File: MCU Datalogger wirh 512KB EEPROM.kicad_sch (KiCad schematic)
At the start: 0 parts

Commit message: Added required symbols for the schematic design.
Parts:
- added BT1: Battery, symbol Device:Battery
- added C1, C2, C3, C4: C, symbol Device:C
- added C5: C_Polarized, symbol Device:C_Polarized
- added D1, D2: LED, symbol Device:LED
- added H1, H2, H3, H4: MountingHole, symbol Mechanical:MountingHole
- added IC1: ~, symbol ATMEGA328P-AU:ATMEGA328P-AU
- added R1, R2, R3, R4, R5, R6: R, symbol Device:R
- added U1, U2: 24LC1025, symbol Memory_EEPROM:24LC1025
- added U3: ~, symbol DS1337S+:DS1337S
- added Y1, Y2: Crystal, symbol Device:Crystal
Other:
- added sheet connectors (connectors.kicad_sch)

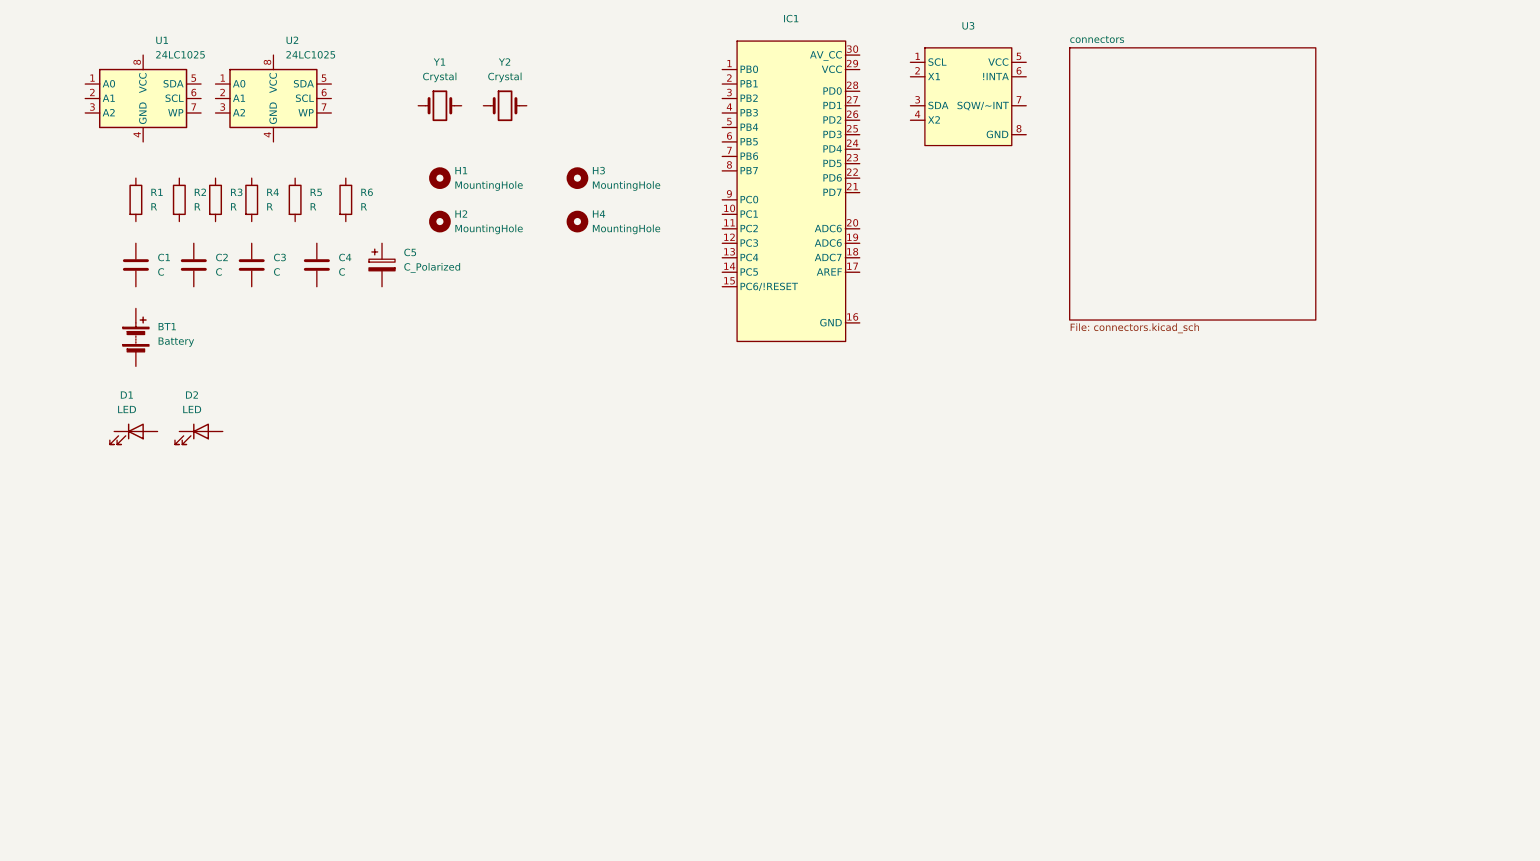
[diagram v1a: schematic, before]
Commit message: Arranged the placement of the symbols.
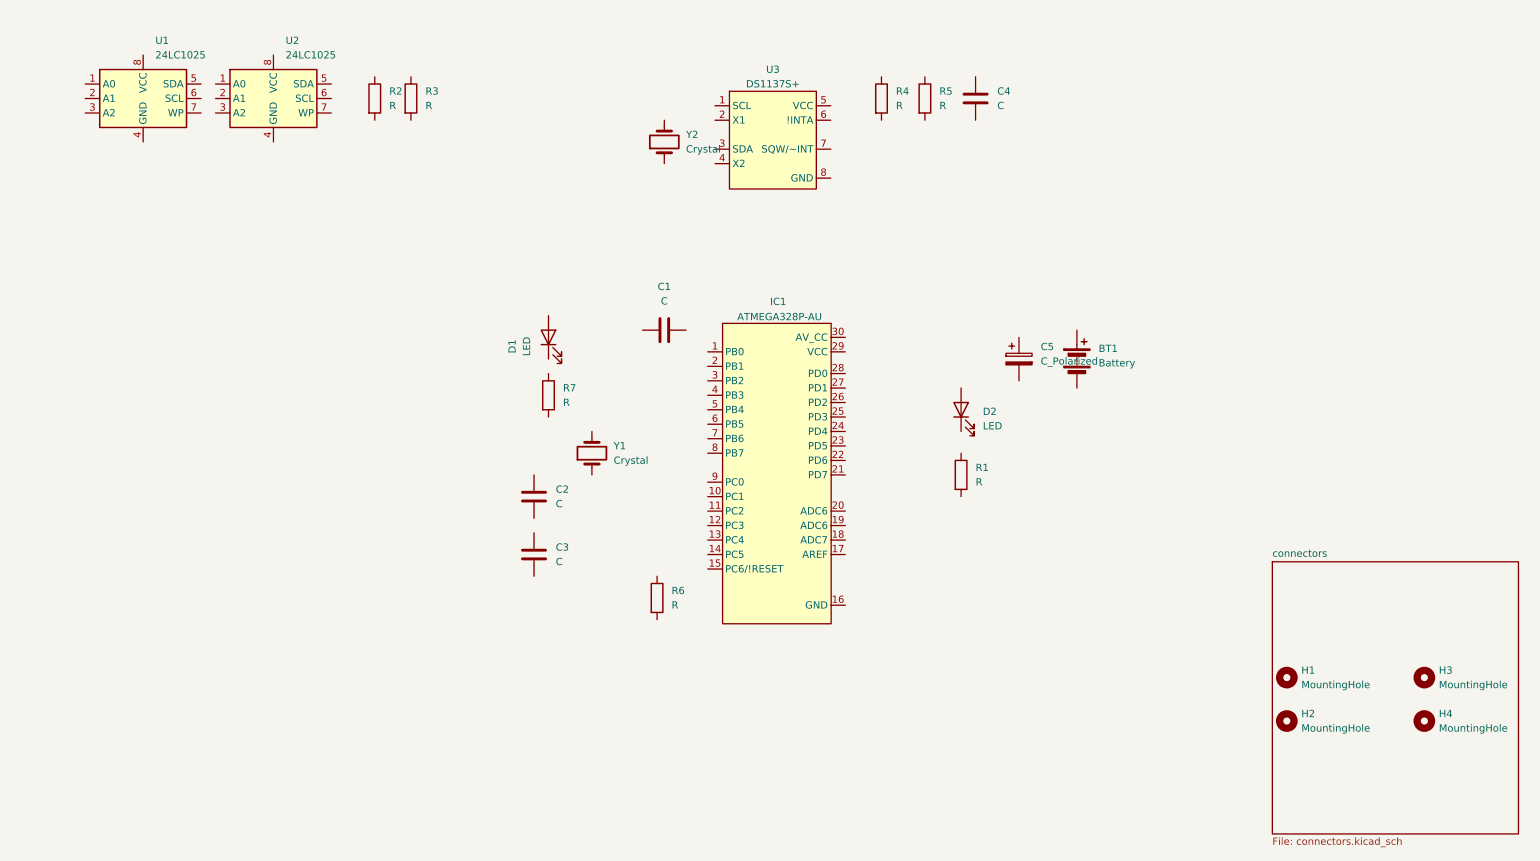
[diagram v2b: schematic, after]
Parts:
- added R7: R, symbol Device:R
- IC1: value ~ -> ATMEGA328P-AU
- U3: value ~ -> DS1137S+
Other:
- moved on the sheet: BT1, C1, C2, C3, C4, C5, D1, D2, H1, H2, H3, H4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

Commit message: Assigned values for each component.
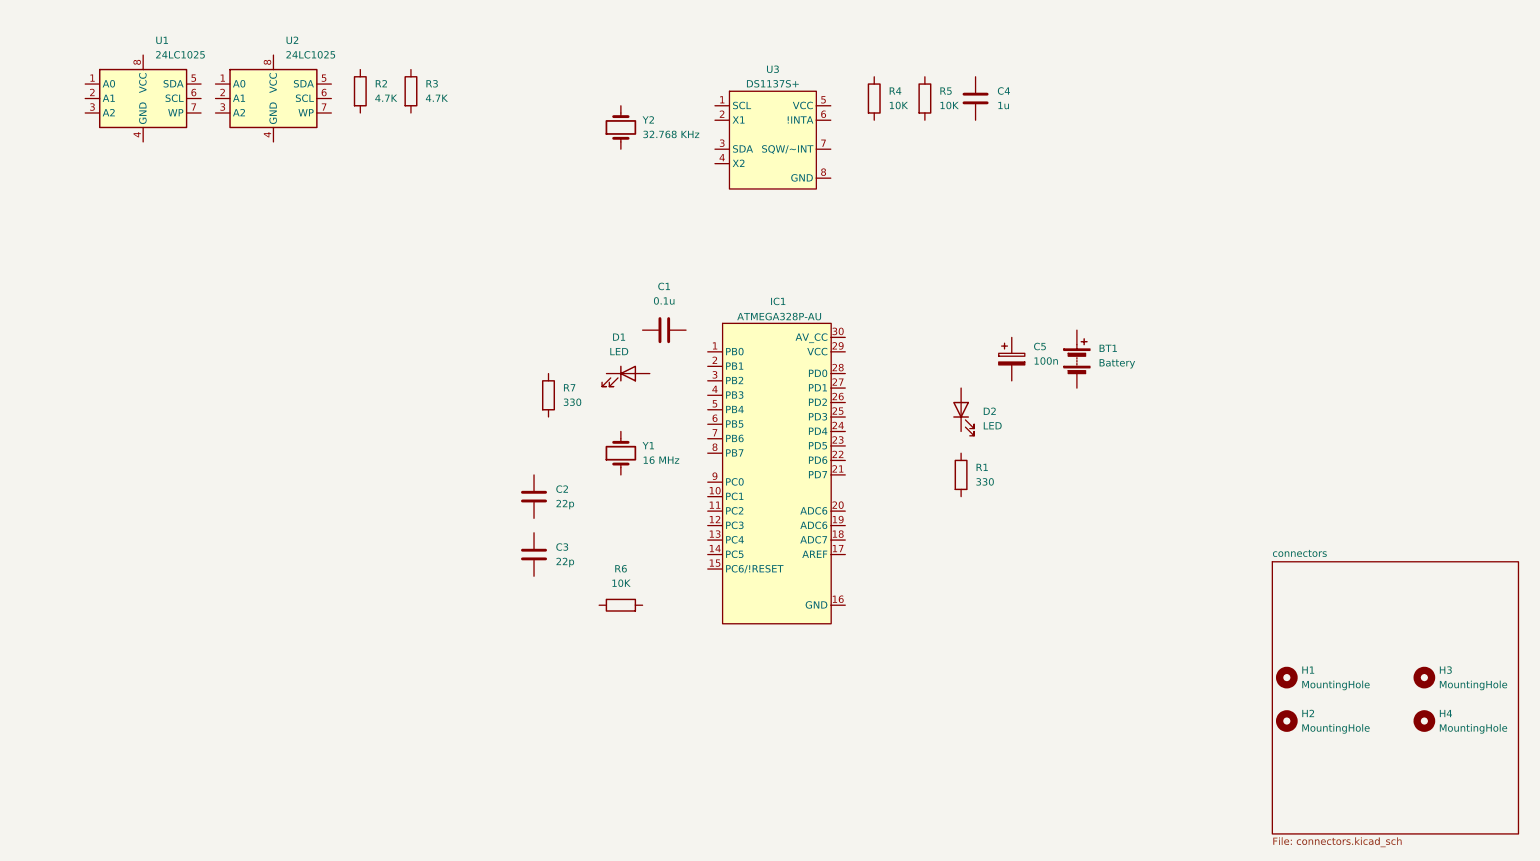
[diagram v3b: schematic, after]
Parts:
- C1: value C -> 0.1u
- C2, C3: value C -> 22p
- C4: value C -> 1u
- C5: value C_Polarized -> 100n
- R1, R7: value R -> 330
- R2, R3: value R -> 4.7K
- R4, R5, R6: value R -> 10K
- Y1: value Crystal -> 16 MHz
- Y2: value Crystal -> 32.768 KHz
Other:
- moved on the sheet: C5, D1, R2, R3, R4, R6, Y1, Y2

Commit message: Assigned footprints to the components in EESchema.
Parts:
- BT1: footprint (none) -> Battery:BatteryHolder_Keystone_1042_1x18650
- C1, C2, C3, C4, C5: footprint (none) -> Capacitor_SMD:C_1206_3216Metric
- D1, D2: footprint (none) -> LED_SMD:LED_1206_3216Metric
- H1, H2, H3, H4: footprint (none) -> MountingHole:MountingHole_2.1mm
- IC1: footprint (none) -> ATMEGA328P-AU:ATMEGA328P-AU
- R1, R2, R3, R4, R5, R6, R7: footprint (none) -> Resistor_SMD:R_0805_2012Metric
- U1, U2: footprint (none) -> Package_SO:SOIC-8_5.3x5.3mm_P1.27mm
- U3: footprint (none) -> DS1337S+:DS1337S+
- Y1, Y2: footprint (none) -> Crystal:Crystal_SMD_5032-2Pin_5.0x3.2mm
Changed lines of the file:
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@@
 			)
 		)
-		(property "Footprint" ""
+		(property "Footprint" "DS1337S+:DS1337S+"
 			(at 144.78 33.02 0)
 			(effects
@@
 			)
 		)
-		(property "Footprint" ""
+		(property "Footprint" "Resistor_SMD:R_0805_2012Metric"
 			(at 111.252 86.36 90)
 			(effects
@@
 			)
 		)
-		(property "Footprint" ""
+		(property "Footprint" "ATMEGA328P-AU:ATMEGA328P-AU"
 			(at 143.51 73.66 0)
 			(effects
@@
 			)
 		)
-		(property "Footprint" ""
+		(property "Footprint" "Crystal:Crystal_SMD_5032-2Pin_5.0x3.2mm"
 			(at 125.73 96.52 0)
 			(effects
@@
 			)
 		)
-		(property "Footprint" ""
+		(property "Footprint" "Capacitor_SMD:C_1206_3216Metric"
 			(at 129.54 75.8952 0)
 			(effects
@@
 			)
 		)
-		(property "Footprint" ""
+		(property "Footprint" "Battery:BatteryHolder_Keystone_1042_1x18650"
 			(at 205.74 78.486 90)
 			(effects
@@
 			)
 		)
-		(property "Footprint" ""
+		(property "Footprint" "Package_SO:SOIC-8_5.3x5.3mm_P1.27mm"
 			(at 41.91 34.29 0)
 			(effects
@@
 			)
 		)
-		(property "Footprint" ""
+		(property "Footprint" "Resistor_SMD:R_0805_2012Metric"
 			(at 125.73 124.968 90)
 			(effects
@@
 			)
 		)
-		(property "Footprint" ""
+		(property "Footprint" "LED_SMD:LED_1206_3216Metric"
 			(at 127 82.55 0)
 			(effects
@@
 			)
 		)
-		(property "Footprint" ""
+		(property "Footprint" "Capacitor_SMD:C_1206_3216Metric"
 			(at 109.5248 100.33 0)
 			(effects
@@
 			)
 		)
-		(property "Footprint" ""
+		(property "Footprint" "Resistor_SMD:R_0805_2012Metric"
 			(at 78.232 33.02 90)
 			(effects
@@
 			)
 		)
-		(property "Footprint" ""
+		(property "Footprint" "MountingHole:MountingHole_2.1mm"
 			(at 266.7 135.89 0)
 			(effects
@@
 			)
 		)
-		(property "Footprint" ""
+		(property "Footprint" "MountingHole:MountingHole_2.1mm"
 			(at 242.57 135.89 0)
 			(effects
@@
 			)
 		)
-		(property "Footprint" ""
+		(property "Footprint" "Resistor_SMD:R_0805_2012Metric"
 			(at 168.402 34.29 90)
 			(effects
@@
 			)
 		)
-		(property "Footprint" ""
+		(property "Footprint" "Resistor_SMD:R_0805_2012Metric"
 			(at 177.292 34.29 90)
 			(effects
@@
 			)
 		)
-		(property "Footprint" ""
+		(property "Footprint" "MountingHole:MountingHole_2.1mm"
 			(at 242.57 143.51 0)
 			(effects
@@
 			)
 		)
-		(property "Footprint" ""
+		(property "Footprint" "Resistor_SMD:R_0805_2012Metric"
 			(at 183.642 100.33 90)
 			(effects
@@
 			)
 		)
-		(property "Footprint" ""
+		(property "Footprint" "Crystal:Crystal_SMD_5032-2Pin_5.0x3.2mm"
 			(at 125.73 39.37 0)
 			(effects
@@
 			)
 		)
-		(property "Footprint" ""
+		(property "Footprint" "MountingHole:MountingHole_2.1mm"
 			(at 266.7 143.51 0)
 			(effects
@@
 			)
 		)
-		(property "Footprint" ""
+		(property "Footprint" "Capacitor_SMD:C_1206_3216Metric"
 			(at 195.2752 83.82 0)
 			(effects
@@
 			)
 		)
-		(property "Footprint" ""
+		(property "Footprint" "LED_SMD:LED_1206_3216Metric"
 			(at 185.42 88.9 0)
 			(effects
@@
 			)
 		)
-		(property "Footprint" ""
+		(property "Footprint" "Resistor_SMD:R_0805_2012Metric"
 			(at 87.122 33.02 90)
 			(effects
@@
 			)
 		)
-		(property "Footprint" ""
+		(property "Footprint" "Package_SO:SOIC-8_5.3x5.3mm_P1.27mm"
 			(at 64.77 34.29 0)
 			(effects
@@
 			)
 		)
-		(property "Footprint" ""
+		(property "Footprint" "Capacitor_SMD:C_1206_3216Metric"
 			(at 109.5248 110.49 0)
 			(effects
@@
 			)
 		)
-		(property "Footprint" ""
+		(property "Footprint" "Capacitor_SMD:C_1206_3216Metric"
 			(at 186.9948 30.48 0)
 			(effects

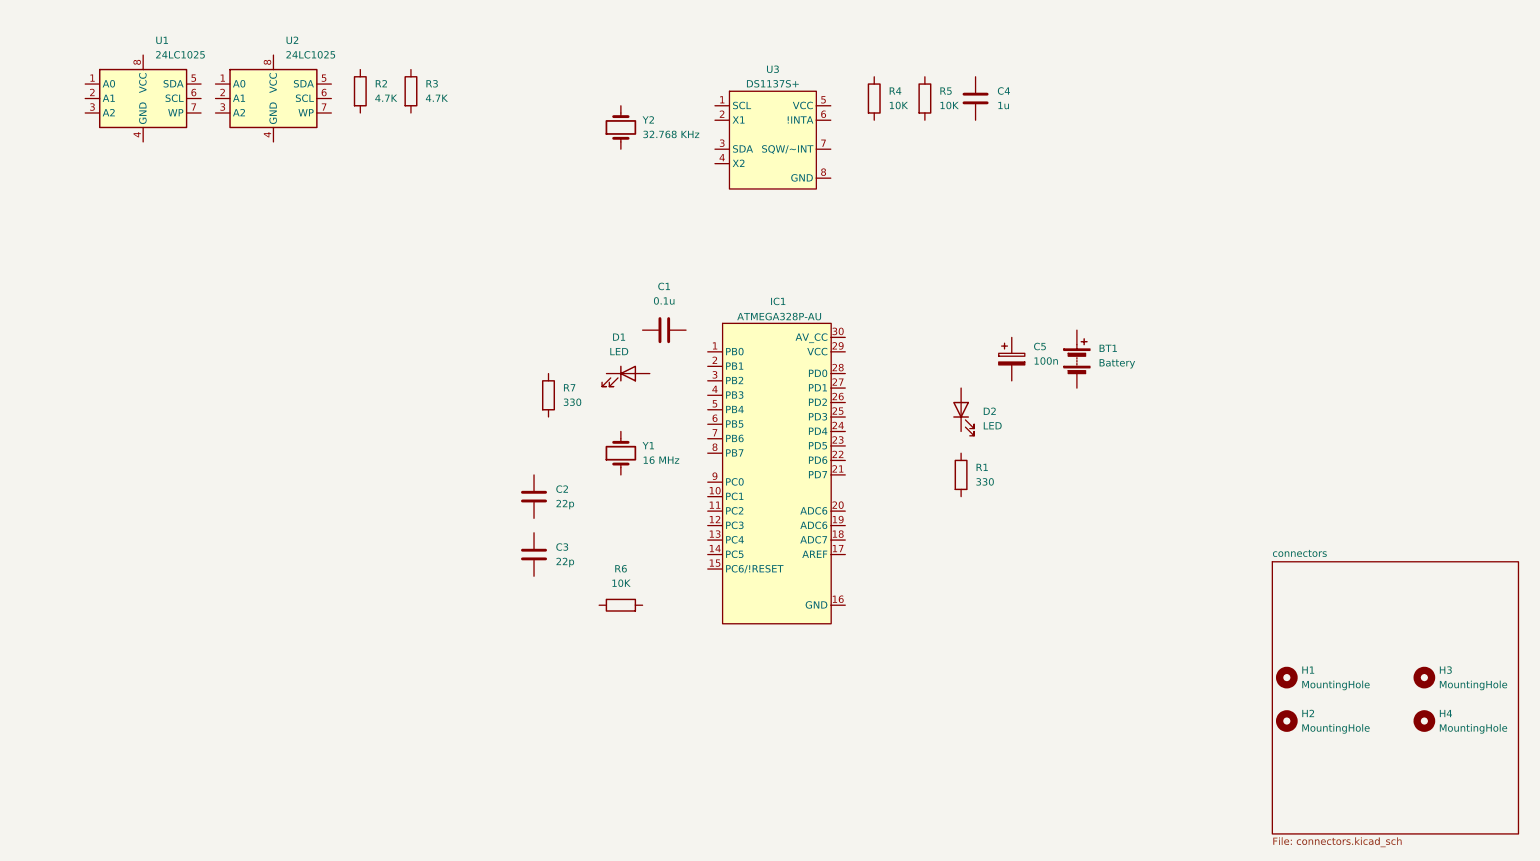
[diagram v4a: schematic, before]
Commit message: Completed the wiring of the main schematic. Next will be the second schematic that contains the connectors.
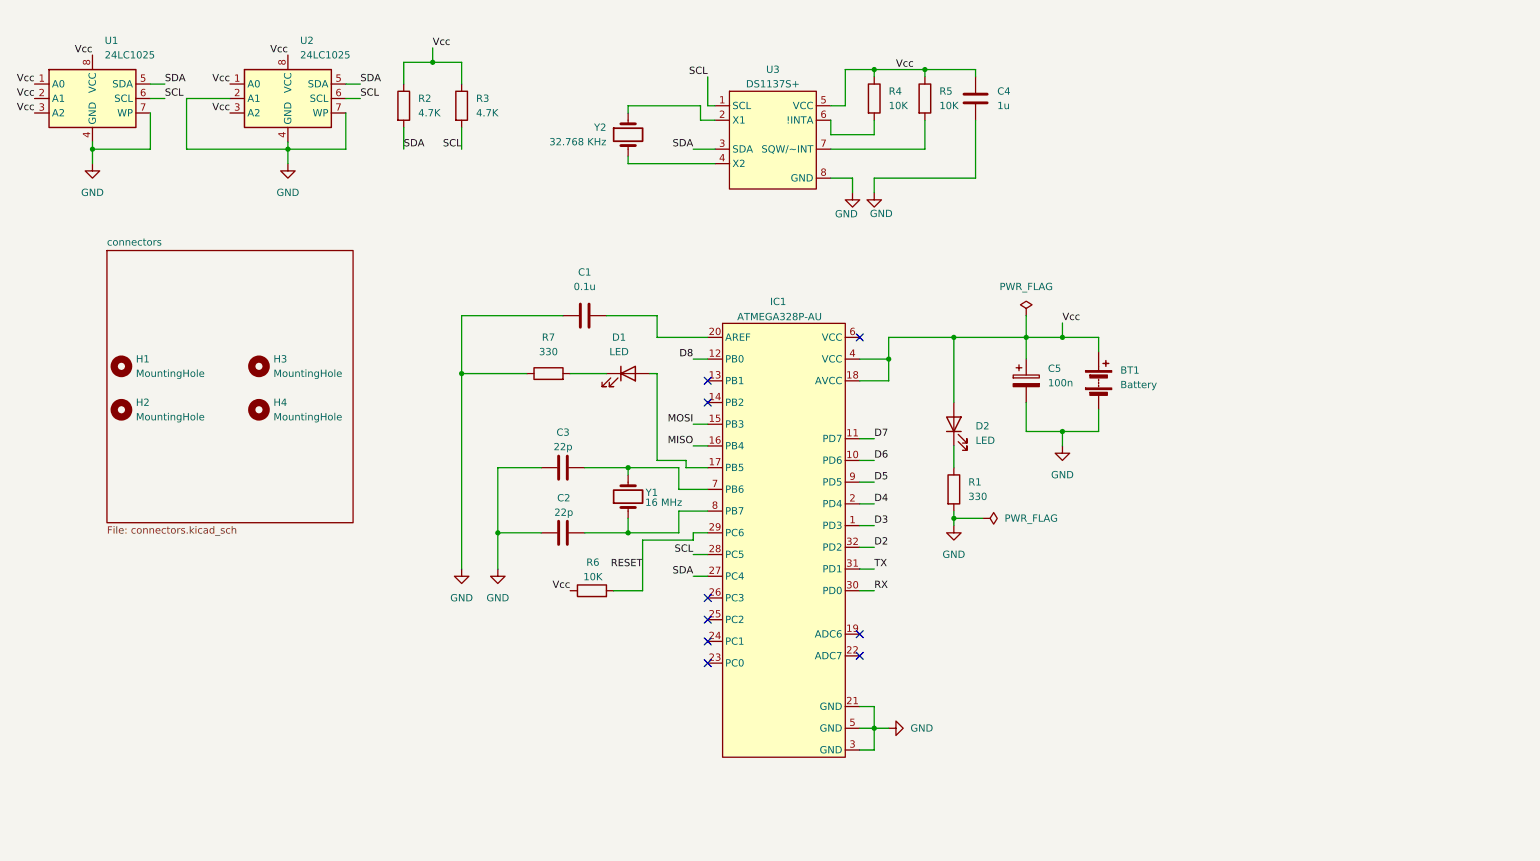
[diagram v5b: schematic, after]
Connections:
- net SCL: now reaches U3.1 (SCL)
- net SCL: now also IC1.28 (PC5), R3.2, U1.6 (SCL), U2.6 (SCL)
- net at U3.2 (X1): now also Y2.1
- net SDA: now reaches U3.3 (SDA)
- net SDA: now also IC1.27 (PC4), R2.2, U1.5 (SDA), U2.5 (SDA)
- net at U3.4 (X2): now also Y2.2
- net Vcc: now reaches U3.5 (VCC)
- net Vcc: now also BT1.1 (+), C4.2, C5.1, D2.2 (A), IC1.18 (AVCC), IC1.4 (VCC), R2.1, R3.1, R4.1, R5.1, R6.1, U1.1 (A0), U1.2 (A1), U1.3 (A2), U1.8 (VCC), U2.1 (A0), U2.3 (A2), U2.8 (VCC)
- net at U3.6 (!INTA): now also R4.2
- net at U3.7 (SQW/~INT): now also R5.2
- net GND: now reaches U3.8 (GND)
- net GND: now also BT1.2 (-), C1.2, C2.1, C3.1, C4.1, C5.2, IC1.21 (GND), IC1.3 (GND), IC1.5 (GND), R1.2, R7.1, U1.4 (GND), U1.7 (WP), U2.2 (A1), U2.4 (GND), U2.7 (WP)
- net at R7.2: now also D1.1 (K)
- net D3: now reaches IC1.1 (PD3)
- net D6: now reaches IC1.10 (PD6)
- net D7: now reaches IC1.11 (PD7)
- net D8: now reaches IC1.12 (PB0)
- net MOSI: now reaches IC1.15 (PB3)
- net MISO: now reaches IC1.16 (PB4)
- net at IC1.17 (PB5): now also D1.2 (A)
- net D4: now reaches IC1.2 (PD4)
- net at IC1.20 (AREF): now also C1.1
- net RESET: now reaches IC1.29 (PC6)
- net RESET: now also R6.2
- net RX: now reaches IC1.30 (PD0)
- net at IC1.7 (PB6): now also C3.2, Y1.2
- net at IC1.8 (PB7): now also C2.2, Y1.1
- net D5: now reaches IC1.9 (PD5)
- net at R1.1: now also D2.1 (K)
- new net D2: IC1.32 (PD2)
- new net TX: IC1.31 (PD1)
- no-connect marks 0 -> 9
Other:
- moved on the sheet: BT1, C1, C2, C3, C5, D2, H1, H2, H3, H4, R1, R2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

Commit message: Finished the wiring of the schematic.
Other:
- sheet connectors ports: added D2, D3, D4, D5, D6, D7, D8, GND, MISO, MOSI, RESET, RX, SCL, SDA, TX, Vcc; removed none
- moved on the sheet: H1, H2, H3, H4
